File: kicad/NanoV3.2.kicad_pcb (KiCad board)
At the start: 2 copper layers, 43.2 x 17.8 mm, 51 parts, among them IC1 FT232RL, IC2 LM1117IMPX-5.0, IC3 ATMEGA328P-AU, J1 Strip15pin, J2 Strip15pin, J3 USB-mini-90 -SMD, J4 ICSP, SW1 157SW, Y1 CSTCE16M0V53-R0

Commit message: updated schematic, not workable yet
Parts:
- removed @HOLE0, @HOLE1, @HOLE2, @HOLE3: , 
- removed C2: 4,7uF_16V, TAN-A
- removed C4, C6, C9: 100nF, C0603-ROUND
- removed D+56, D-56: DNP, TP-1.00MM
- removed D1: SS1P3L, DO220AAL
- removed F1: MFFSMF050, 0603-1608X90N
- removed IC1: FT232RL, SSOP28
- removed J1, J2: Strip15pin, HEAD15-NOSS
- removed J3: USB-mini-90 -SMD, USB-MINI-B_2
- removed L56: Yellow, CHIPLED_0805
- removed RP2: 1K, CAY16
- removed RX56: Red, CHIPLED_0805
- removed TX56: Green, CHIPLED_0805
- removed U$4, U$5, U$53, U$54: DNP, FD-1-1.5
- removed VP_0, VP_1, VP_10, VP_11, VP_12, VP_13, VP_2, VP_3, VP_4, VP_5, VP_6, VP_7, VP_8, VP_9: VPDEV0, VPAC0
- added P1: CONN_01X03, Pin_Headers:Pin_Header_Straight_1x03, F.Cu at (144.8, 111.8)
- C1, C3, C5, C7, C8, IC2, RP1: moved to F.Cu
- J4: value ICSP -> ~
- SW1: value 157SW -> RESET
- Y1: value CSTCE16M0V53-R0 -> 16MHz
- moved C8 24.3 mm to (134.6, 97.8)
- moved J4 21.0 mm to (147.3, 99.1), turned to 0 degrees
- moved C7 20.7 mm to (137.2, 111.8)
- moved C3 19.9 mm to (129.5, 97.8), turned to 180 degrees
- moved PWR56 13.8 mm to (142.2, 104.1), turned to 0 degrees
- moved C5 13.4 mm to (146.1, 108.0)
- moved IC2 10.7 mm to (149.9, 104.1), turned to 90 degrees
- moved RP1 9.95 mm to (140.7, 109.7)
- moved SW1 9.52 mm to (152.8, 112.4), turned to 90 degrees
- moved IC3 9.06 mm to (133.3, 105.4)
- moved Y1 8.60 mm to (139.3, 99.2), turned to 135 degrees
- moved C1 4.45 mm to (129.5, 111.8), turned to 0 degrees
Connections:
- net AREF renamed /AREF
- net D0/RX renamed /D0/RX
- net D1/TX renamed /D1/TX
- net D11/MOSI renamed /D11/MOSI
- net D12/MISO renamed /D12/MISO
- net D13/SCK renamed /D13/SCK
- net N$1 renamed /N$1
- net N$2 renamed /N$2
- net N$3 renamed /N$3
- net RESET renamed /RESET
- IC2 pad 3: VIN -> (no net)
- IC3 pad 1: D3 -> (no net)
- IC3 pad 10: D6 -> (no net)
- IC3 pad 11: D7 -> (no net)
- IC3 pad 12: D8 -> (no net)
- IC3 pad 13: D9 -> (no net)
- IC3 pad 14: D10 -> (no net)
- IC3 pad 19: A6 -> (no net)
- IC3 pad 2: D4 -> (no net)
- IC3 pad 22: A7 -> (no net)
- IC3 pad 23: A0 -> (no net)
- IC3 pad 24: A1 -> (no net)
- IC3 pad 25: A2 -> (no net)
- IC3 pad 26: A3 -> (no net)
- IC3 pad 27: A4 -> (no net)
- IC3 pad 28: A5 -> (no net)
- IC3 pad 32: D2 -> (no net)
- IC3 pad 9: D5 -> (no net)
- RP1 pad 7: TX -> /TX
- RP1 pad 8: RX -> Net-(P1-Pad2)
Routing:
- net COM: track 10.4 -> 69.9 mm
- net /D13/SCK: track 55.6 -> 0.00 mm, vias 3 -> 0
- net /D12/MISO: track 54.3 -> 0.00 mm
- net /D11/MOSI: track 45.6 -> 0.00 mm
- net VUSB: track 40.3 -> 0.00 mm, vias 2 -> 0
- net /RESET: track 56.7 -> 19.7 mm, vias 3 -> 0
- net +5V: track 84.0 -> 47.9 mm, vias 5 -> 0
- net /D1/TX: track 33.0 -> 3.44 mm, vias 1 -> 0
- net /D0/RX: track 33.4 -> 8.33 mm, vias 2 -> 0
- net A6: track 23.6 -> 0.00 mm, vias 1 -> 0
- net A7: track 21.0 -> 0.00 mm, vias 1 -> 0
- net 3V3: track 20.4 -> 0.00 mm
- net N$5: track 16.0 -> 0.00 mm, vias 1 -> 0
- net TX: track 14.5 -> 0.00 mm
- net N$6: track 14.5 -> 0.00 mm, vias 1 -> 0
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
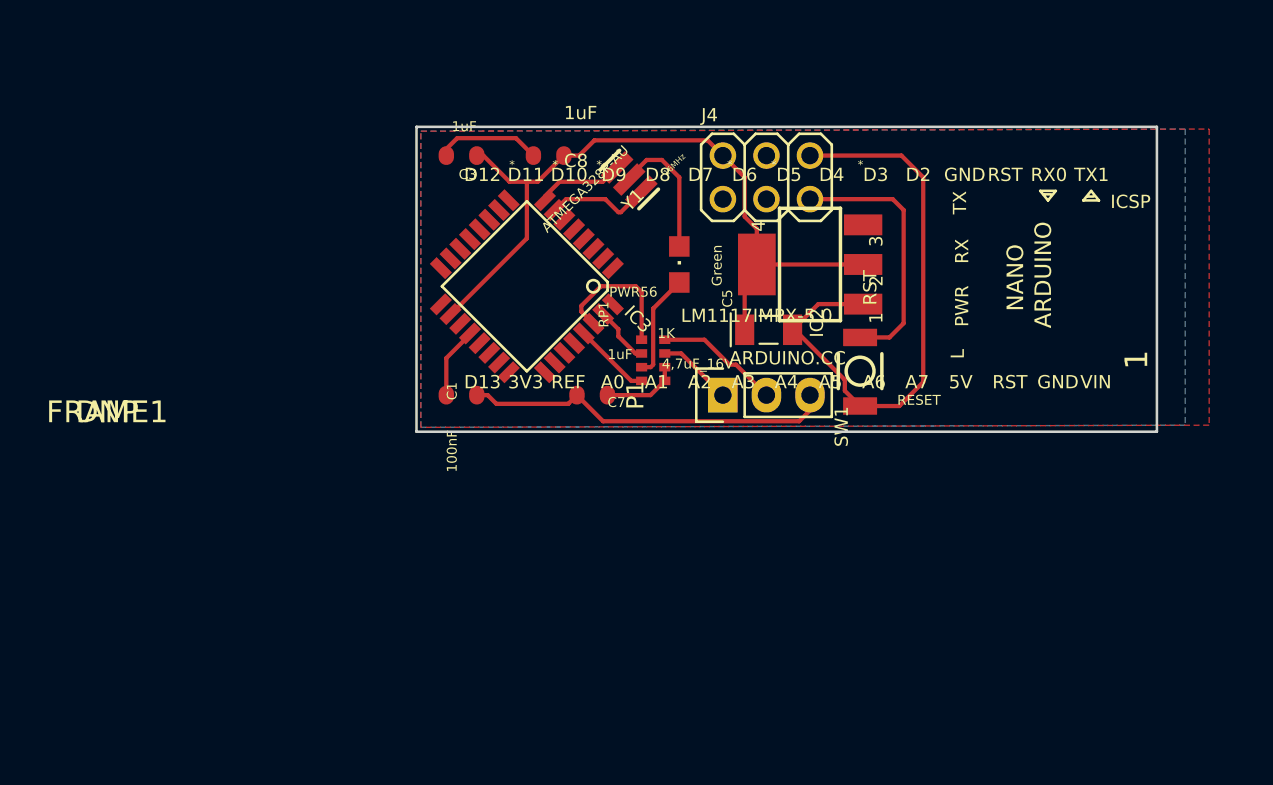
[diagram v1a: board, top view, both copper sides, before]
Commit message: updated libs and deleted reset button
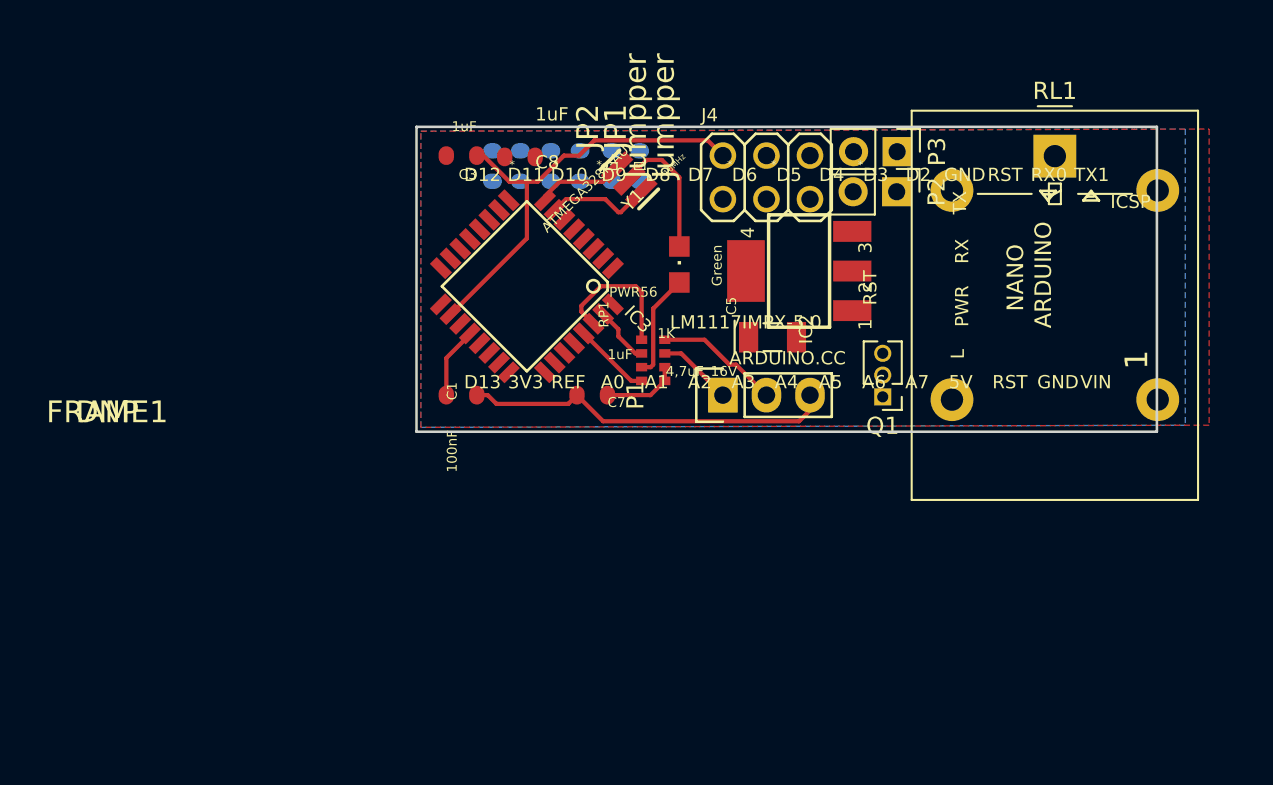
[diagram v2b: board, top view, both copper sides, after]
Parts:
- removed SW1: RESET, SMD_157SW
- added JP1: Jumpper, C0603-ROUND, F.Cu at (139.9, 98.4)
- added JP2: Jumpper, C0603-ROUND, F.Cu at (138.3, 98.4)
- added JP3: Jumpper, C0603-ROUND, B.Cu at (136.4, 98.4)
- added JP4: Jumpper, C0603-ROUND, B.Cu at (134.7, 98.4)
- added JP5: Jumpper, C0603-ROUND, B.Cu at (133.0, 98.4)
- added JP6: Jumpper, C0603-ROUND, B.Cu at (131.3, 98.4)
- added P2: OUT, Pin_Headers:Pin_Header_Straight_1x02_Pitch2.54mm, F.Cu at (154.9, 99.9)
- added P3: INPUT, Pin_Headers:Pin_Header_Straight_1x02_Pitch2.54mm, F.Cu at (154.9, 97.6)
- added Q1: BC237, Pin_Headers:Pin_Header_Straight_1x03_Pitch1.27mm, F.Cu at (154.1, 111.9)
- added RL1: FINDER-40.31, autoSwitch:Relay_SPDT_OMRON-G5LE-1, F.Cu at (164.1, 97.8)
- P1: value CONN_01X03 -> TTL
- moved C8 1.68 mm to (132.9, 97.9)
- moved IC2 0.74 mm to (149.2, 104.5)
- moved C5 0.49 mm to (146.3, 108.4)
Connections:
- IC2 pad 3: (no net) -> VIN
- IC3 pad 1: (no net) -> /D3
- IC3 pad 10: (no net) -> /D6
- IC3 pad 11: (no net) -> /D7
- IC3 pad 12: (no net) -> /D8
- IC3 pad 13: (no net) -> /D9
- IC3 pad 2: (no net) -> /D4
- IC3 pad 32: (no net) -> /D2
- IC3 pad 9: (no net) -> /D5
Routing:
- net COM: track 69.9 -> 29.9 mm
- net +5V: track 47.9 -> 30.4 mm
- net /RESET: track 19.7 -> 4.52 mm

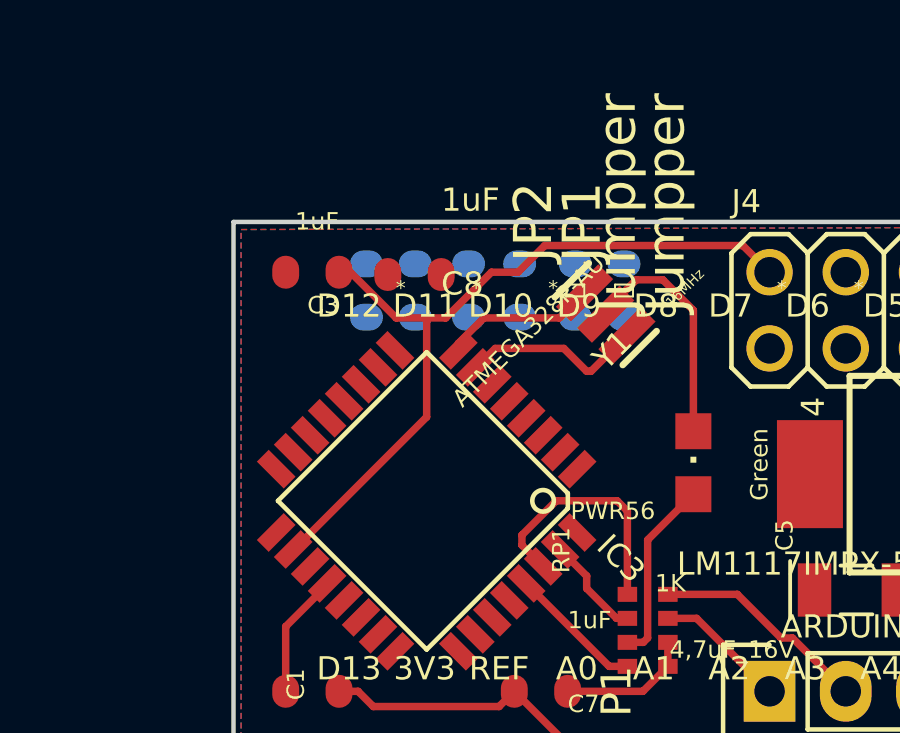
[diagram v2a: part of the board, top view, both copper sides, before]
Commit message: moved some components to back
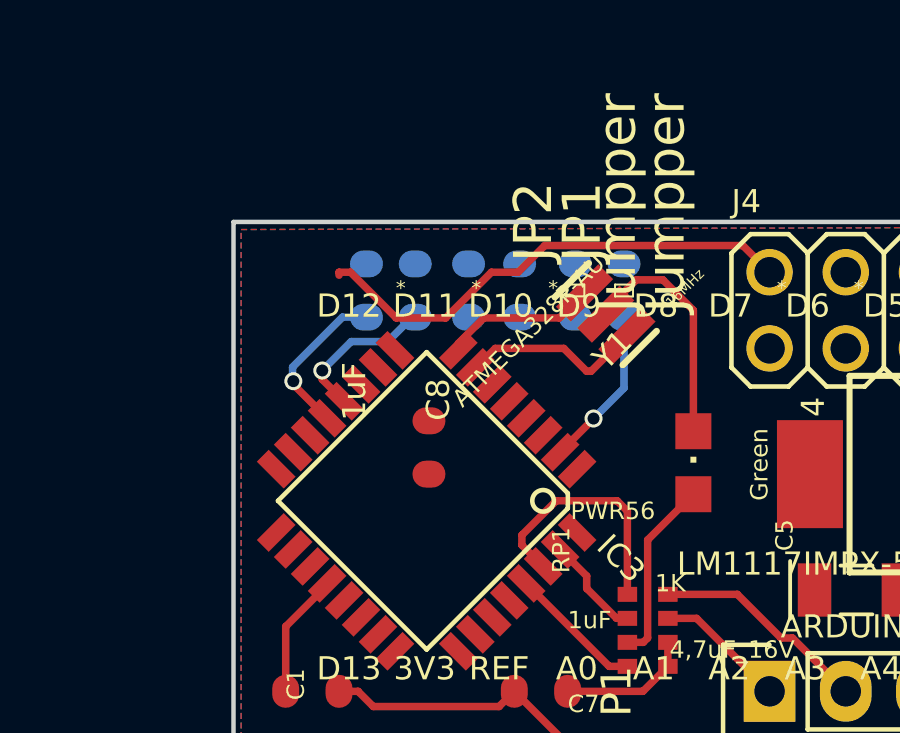
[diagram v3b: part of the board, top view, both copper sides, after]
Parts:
- removed C3: 1uF, C0603-ROUND
- moved C8 5.79 mm to (133.4, 103.6), turned to 270 degrees
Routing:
- net +5V: track 30.4 -> 21.1 mm
- net /D4: track 0.00 -> 5.38 mm, vias 0 -> 1
- net /D9: track 0.00 -> 5.34 mm, vias 0 -> 1
- net /D8: track 0.00 -> 5.16 mm, vias 0 -> 1

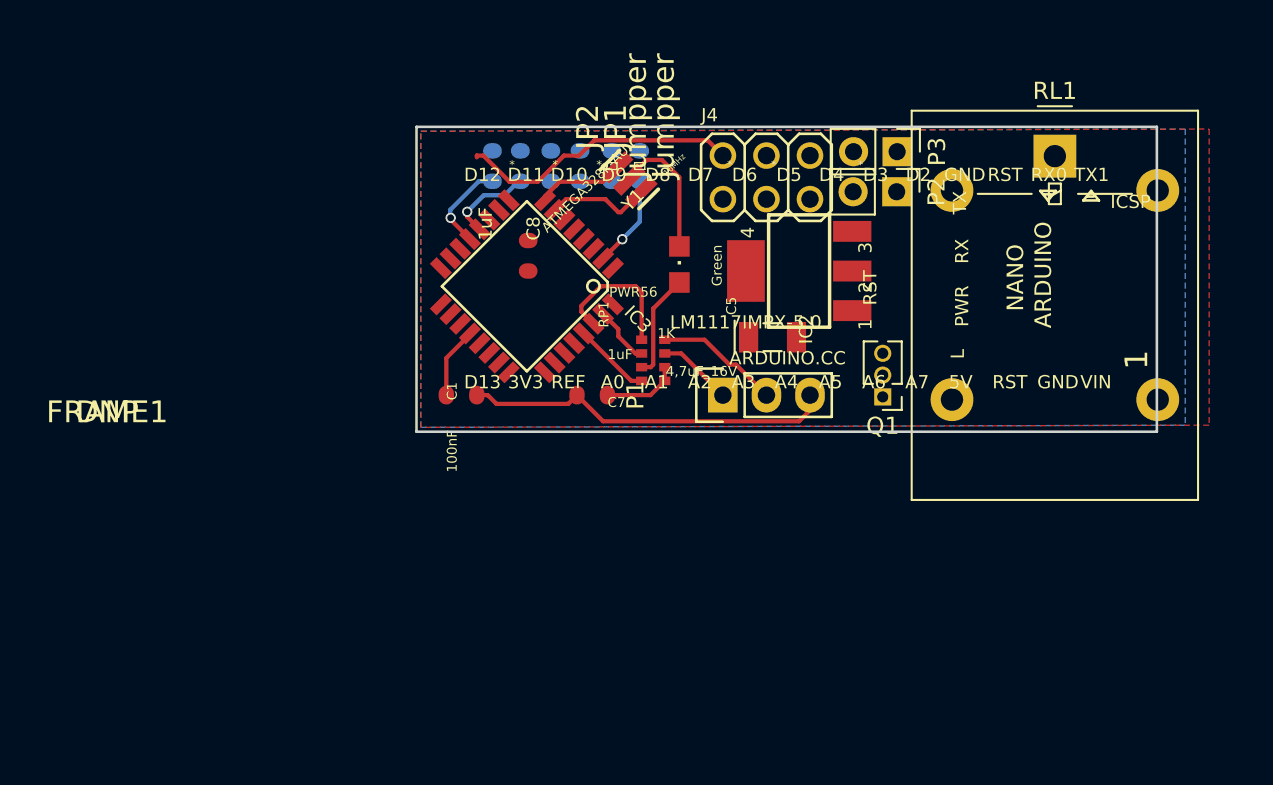
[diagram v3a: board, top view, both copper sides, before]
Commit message: moved components to right position and clean up marks
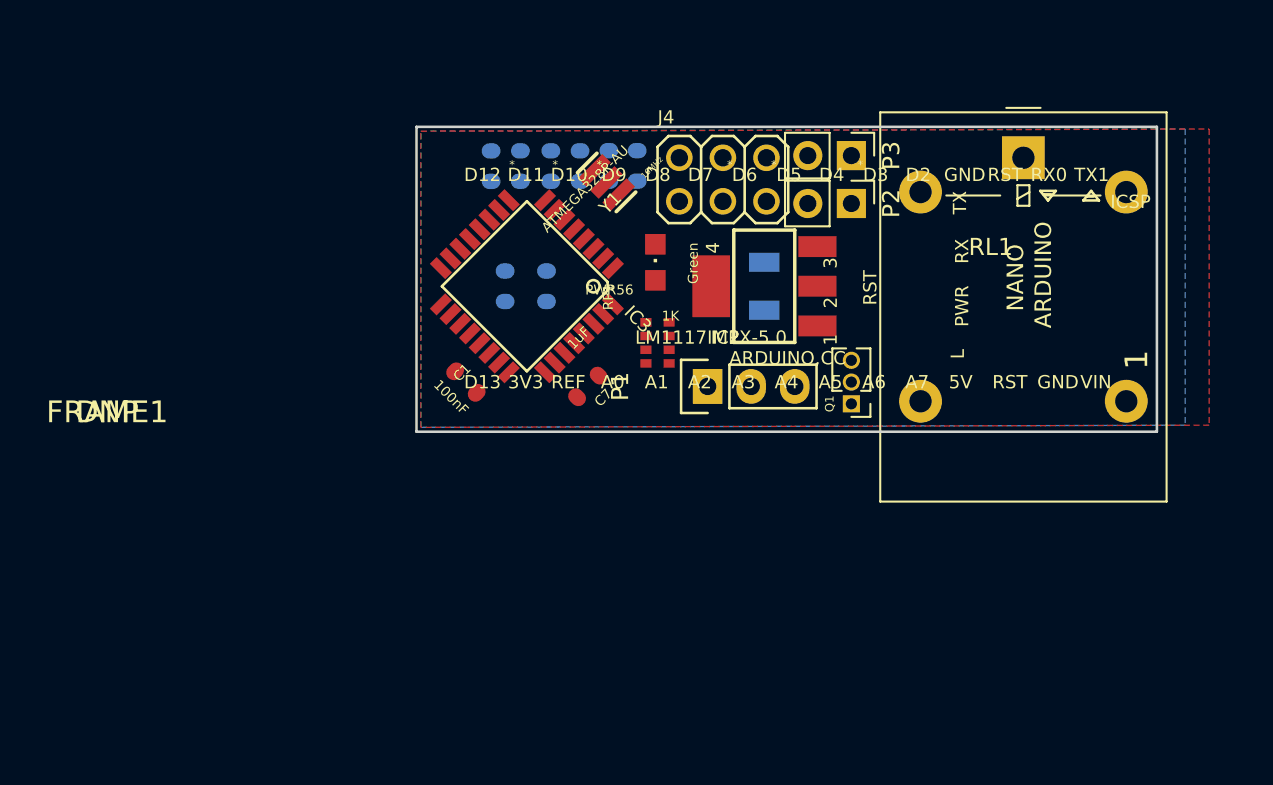
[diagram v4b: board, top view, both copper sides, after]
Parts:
- added C3: 1uF, C0603-ROUND, B.Cu at (134.5, 105.4)
- C5, C8, JP1, JP2: moved to B.Cu
- moved P2 2.73 mm to (152.3, 100.6)
- moved P3 2.68 mm to (152.3, 97.8)
- moved J4 2.54 mm to (144.8, 99.2)
- moved C8 2.23 mm to (132.1, 105.4)
- moved IC2 2.22 mm to (147.2, 105.4)
- moved Q1 1.87 mm to (152.3, 112.3)
- moved RL1 1.84 mm to (162.3, 97.9)
- moved C5 1.82 mm to (147.2, 106.8), turned to 90 degrees
- moved PWR56 1.40 mm to (140.8, 104.0)
- moved Y1 1.33 mm to (138.0, 99.4)
- moved RP1 1.05 mm to (141.0, 108.7)
- moved P1 1.02 mm to (143.9, 111.3)
- moved C1 0.80 mm to (129.8, 111.0), turned to 315 degrees
- moved C7 0.57 mm to (136.9, 111.3), turned to 225 degrees
- moved JP2 0.17 mm to (138.1, 98.4)
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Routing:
- net COM: track 29.6 -> 0.00 mm
- net +5V: track 21.1 -> 0.00 mm
- net /D0/RX: track 8.33 -> 0.00 mm
- net Net-(P1-Pad2): track 7.27 -> 0.00 mm
- net /N$3: track 6.16 -> 0.00 mm
- net /N$2: track 6.13 -> 0.00 mm
- net /D4: track 5.38 -> 0.00 mm, vias 1 -> 0
- net /D9: track 5.34 -> 0.00 mm, vias 1 -> 0
- net /D8: track 5.16 -> 0.00 mm, vias 1 -> 0
- net /N$1: track 5.14 -> 0.00 mm
- net /RESET: track 4.52 -> 0.00 mm
- net /TX: track 4.40 -> 0.00 mm
- net /AREF: track 4.17 -> 0.00 mm
- net /D1/TX: track 3.44 -> 0.00 mm

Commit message: moved components to right position and clean up marks
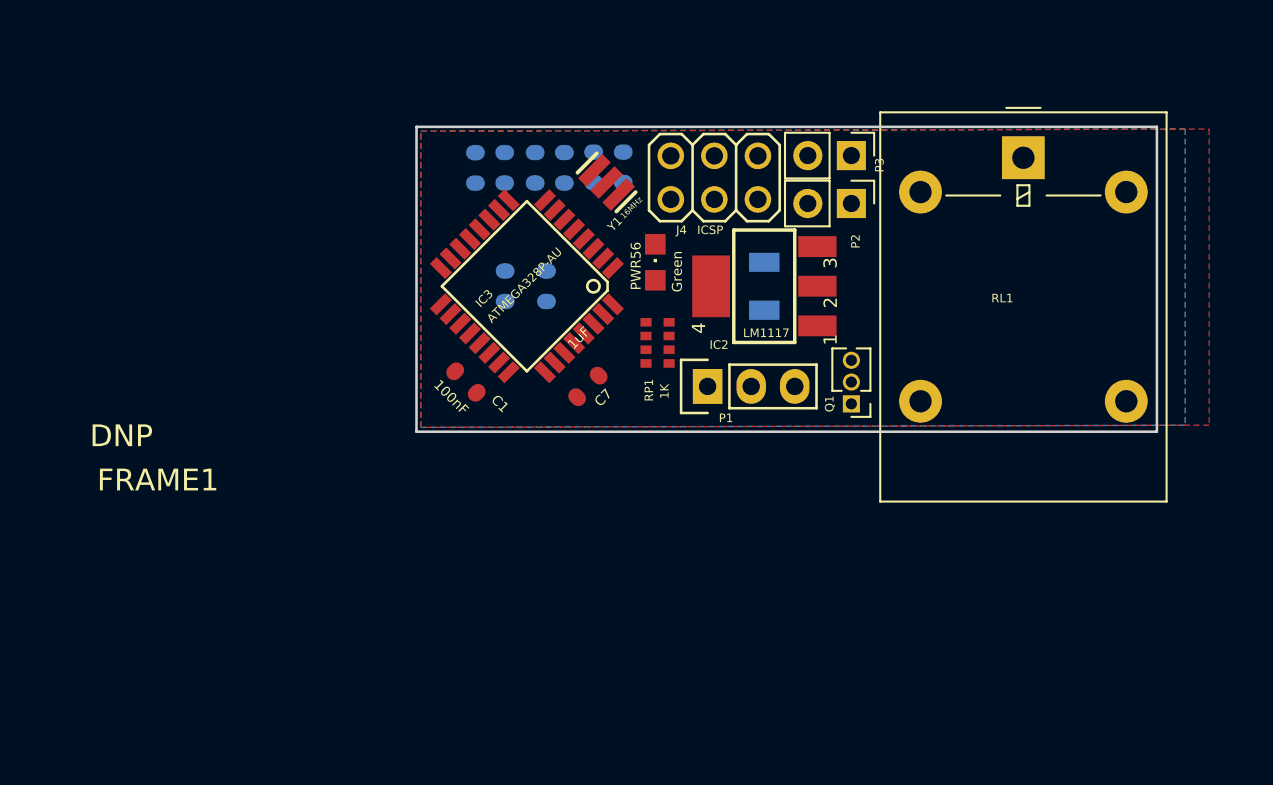
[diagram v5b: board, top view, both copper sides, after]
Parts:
- IC2: value LM1117IMPX-5.0 -> LM1117
- P3: value INPUT -> IN
- moved JP6 0.92 mm to (130.3, 98.5)
- moved JP3 0.92 mm to (135.5, 98.5)
- moved JP4 0.92 mm to (133.8, 98.5)
- moved JP5 0.92 mm to (132.1, 98.5)
- moved JP2 0.89 mm to (137.2, 98.5)
- moved JP1 0.82 mm to (139.0, 98.5)
- moved J4 0.51 mm to (144.3, 99.1)
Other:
- board text removed: "*"
- board text removed: "1"
- board text removed: "3V3"
- board text removed: "5V"
- board text removed: "A0"
- board text removed: "A1"
- board text removed: "A2"
- board text removed: "A3"
- board text removed: "A4"
- board text removed: "A5"
- board text removed: "A6"
- board text removed: "A7"
- board text removed: "ARDUINO"
- board text removed: "ARDUINO.CC"
- board text removed: "D10"
- board text removed: "D11"
- board text removed: "D12"
- board text removed: "D13"
- board text removed: "D2"
- board text removed: "D3"
- board text removed: "D4"
- board text removed: "D5"
- board text removed: "D6"
- board text removed: "D7"
- board text removed: "D8"
- board text removed: "D9"
- board text removed: "GND"
- board text removed: "L"
- board text removed: "NANO"
- board text removed: "PWR"
- board text removed: "REF"
- board text removed: "RST"
- board text removed: "RX"
- board text removed: "RX0"
- board text removed: "TX"
- board text removed: "TX1"
- board text removed: "VIN"

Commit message: finished layout
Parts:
- IC2: value LM1117 -> LM1117IMPX-5.0
- JP1, JP2, JP3, JP4, JP5, JP6: value Jumpper -> ~
- P3: value IN -> INPUT
- RL1: value FINDER-40.31 -> ~; footprint autoSwitch:Relay_SPDT_OMRON-G5LE-1 -> autoSwitch:Relay_HK4100F
- moved P3 17.5 mm to (167.5, 106.3), turned to 0 degrees
- moved P2 15.3 mm to (167.5, 100.4), turned to 0 degrees
- moved RL1 13.3 mm to (163.5, 111.1), turned to 90 degrees
- moved J4 2.32 mm to (146.6, 99.2)
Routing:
- net +5V: track 0.00 -> 61.0 mm, vias 0 -> 4
- net COM: track 0.00 -> 51.1 mm, vias 0 -> 1
- net /RESET: track 0.00 -> 32.5 mm, vias 0 -> 3
- net /D11/MOSI: track 0.00 -> 27.4 mm, vias 0 -> 3
- net VIN: track 0.00 -> 25.1 mm
- net /D13/SCK: track 0.00 -> 24.5 mm, vias 0 -> 1
- net /D12/MISO: track 0.00 -> 21.5 mm, vias 0 -> 1
- net /D2: track 0.00 -> 20.7 mm, vias 0 -> 1
- net /D3: track 0.00 -> 16.9 mm, vias 0 -> 1
- net Net-(P1-Pad2): track 0.00 -> 12.0 mm, vias 0 -> 1
- net /D5: track 0.00 -> 9.07 mm, vias 0 -> 1
- net /D0/RX: track 0.00 -> 6.64 mm
- net /D6: track 0.00 -> 5.87 mm, vias 0 -> 1
- net /D4: track 0.00 -> 5.23 mm, vias 0 -> 1
- net /D7: track 0.00 -> 4.97 mm, vias 0 -> 1
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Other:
- net class w0.5 added: clearance 0.4, trace_width 0.5, via_dia 1.2, via_drill 0.8

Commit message: finished layout
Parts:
- IC2: value LM1117IMPX-5.0 -> LM1117
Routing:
- net /RESET: track 32.5 -> 20.1 mm, vias 3 -> 1
- net COM: track 51.1 -> 52.0 mm
- net +5V: track 61.0 -> 60.4 mm
- net /D12/MISO: track 21.5 -> 20.9 mm
